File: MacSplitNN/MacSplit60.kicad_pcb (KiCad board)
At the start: 2 copper layers, 166.1 x 112 mm, 73 parts, among them J1 USB_C_Receptacle_USB2.0, SW1 SW_Push, SW10 SW_Push, SW100 SW_SPST, SW11 SW_Push, SW12 SW_Push, SW13 SW_Push, SW14 SW_Push, SW15 SW_Push, SW16 SW_Push, SW17 SW_Push, SW18 SW_Push, SW19 SW_Push, SW2 SW_Push, SW20 SW_Push, SW21 SW_Push, SW22 SW_Push, SW23 SW_Push, SW24 SW_Push, SW25 SW_Push, SW26 SW_Push, SW27 SW_Push, SW28 SW_Push, SW29 SW_Push, SW3 SW_Push, SW30 SW_Push, SW4 SW_Push, SW5 SW_Push, SW6 SW_Push, SW7 SW_Push, SW8 SW_Push, SW9 SW_Push, U1 Pico, U2 MCP23S17_ML

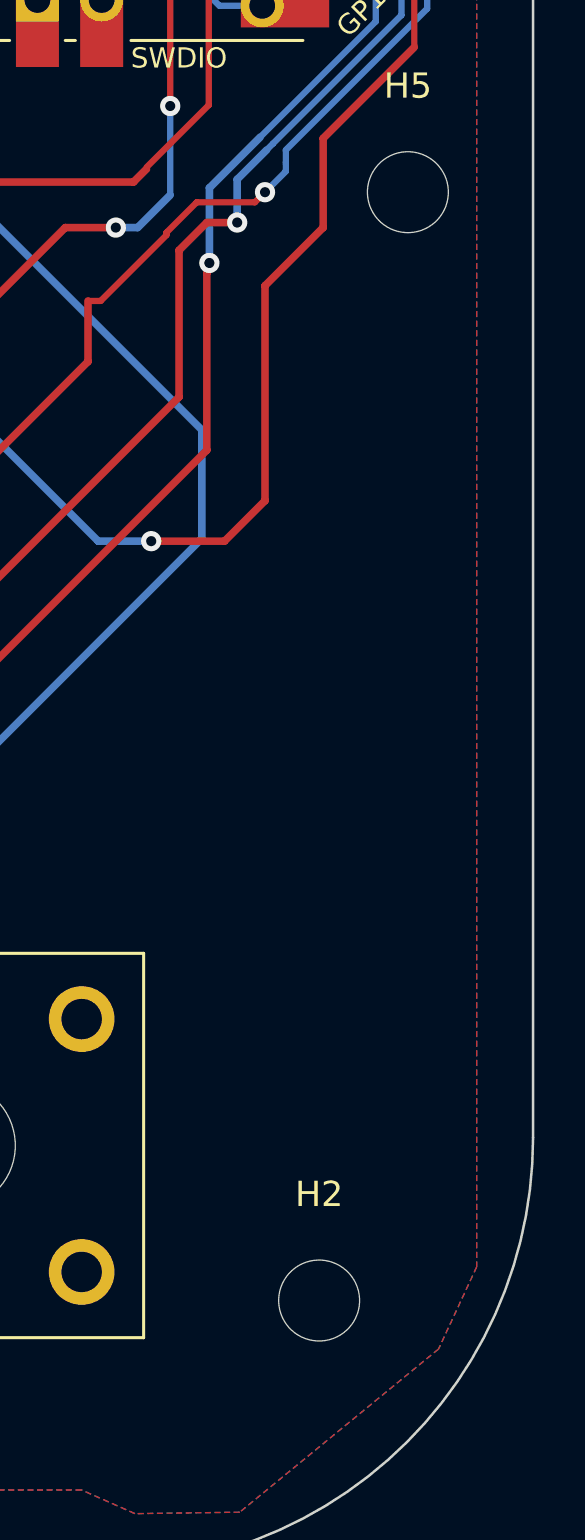
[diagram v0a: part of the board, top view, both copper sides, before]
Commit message: Adds PCB design info to silkscreen, gerbers for production
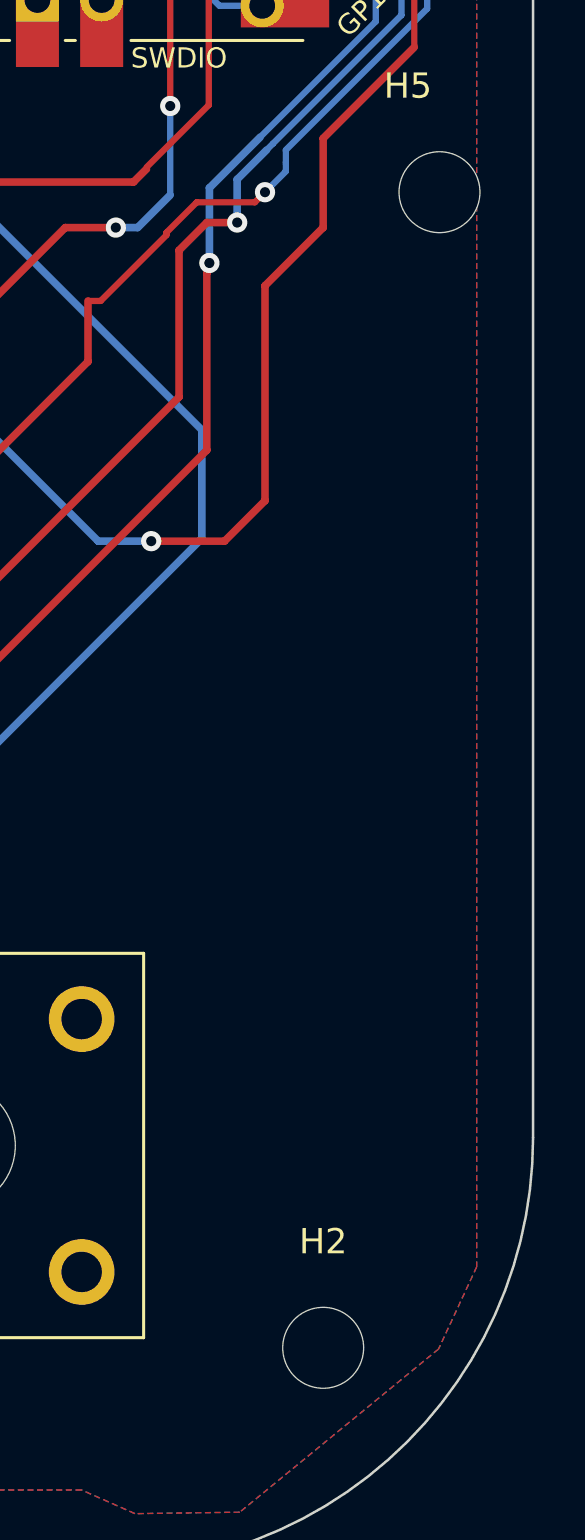
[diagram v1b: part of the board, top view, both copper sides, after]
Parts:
- moved H2 1.88 mm to (244.3, 138.3)
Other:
- board text added: "MacSplit60 Keyboard by Neeraj Adsul Copyright 2022, 125 Systems. Revision 1"
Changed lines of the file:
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@@
       (outputformat 1)
       (mirror false)
-      (drillshape 1)
+      (drillshape 0)
       (scaleselection 1)
       (outputdirectory "")
@@
   )
   (footprint "MountingHole:MountingHole_3.2mm_M3" (layer "F.Cu")
-    (at 244.14 136.43)
+    (at 244.3 138.3)
     (descr "Mounting Hole 3.2mm, no annular, M3")
     (tags "mounting hole 3.2mm no annular m3")
@@
     (fp_circle (center 0 0) (end 3.2 0) (layer "Cmts.User") (width 0.15) (fill none))
     (fp_circle (center 0 0) (end 3.45 0) (layer "F.CrtYd") (width 0.05) (fill none))
-    (pad "" np_thru_hole circle (at 0 0) (size 3.2 3.2) (drill 3.2) (layers *.Cu *.Mask))
+    (pad "" np_thru_hole circle (at 1.25 0) (size 3.2 3.2) (drill 3.2) (layers F&B.Cu *.Mask))
   )
   (footprint "Switch_Keyboard_Kailh:SW_Kailh_Choc_V1V2_1.00u" (layer "F.Cu")
@@
       (effects (font (size 1 1) (thickness 0.15)))
     )
-    (fp_text user "${REFERENCE}" (at 0 0) (layer "F.Fab")
+    (fp_text user "${REFERENCE}" (at 0 -1.2825) (layer "F.Fab")
       (effects (font (size 1 1) (thickness 0.15)))
     )
@@
     (fp_line (start -3 2) (end -2 3) (layer "B.Fab") (width 0.1))
     (fp_line (start 3 3) (end 3 -3) (layer "B.Fab") (width 0.1))
-    (pad "" smd roundrect (at 1.42 1.42) (size 1.14 1.14) (layers "B.Paste") (roundrect_rratio 0.219298))
-    (pad "" smd roundrect (at 1.42 0) (size 1.14 1.14) (layers "B.Paste") (roundrect_rratio 0.219298))
-    (pad "" smd roundrect (at 1.42 -1.42) (size 1.14 1.14) (layers "B.Paste") (roundrect_rratio 0.219298))
-    (pad "" smd roundrect (at 0 0) (size 1.14 1.14) (layers "B.Paste") (roundrect_rratio 0.219298))
-    (pad "" smd roundrect (at -1.42 1.42) (size 1.14 1.14) (layers "B.Paste") (roundrect_rratio 0.219298))
-    (pad "" smd roundrect (at 0 1.42) (size 1.14 1.14) (layers "B.Paste") (roundrect_rratio 0.219298))
-    (pad "" smd roundrect (at -1.42 -1.42) (size 1.14 1.14) (layers "B.Paste") (roundrect_rratio 0.219298))
-    (pad "" smd roundrect (at -1.42 0) (size 1.14 1.14) (layers "B.Paste") (roundrect_rratio 0.219298))
-    (pad "" smd roundrect (at 0 -1.42) (size 1.14 1.14) (layers "B.Paste") (roundrect_rratio 0.219298))
+    (pad "" smd roundrect (at 1.42 1.42) (size 1.14 1.14) (layers "B.Paste") (roundrect_rratio 0.2192982456))
+    (pad "" smd roundrect (at 1.42 0) (size 1.14 1.14) (layers "B.Paste") (roundrect_rratio 0.2192982456))
+    (pad "" smd roundrect (at 1.42 -1.42) (size 1.14 1.14) (layers "B.Paste") (roundrect_rratio 0.2192982456))
+    (pad "" smd roundrect (at 0 0) (size 1.14 1.14) (layers "B.Paste") (roundrect_rratio 0.2192982456))
+    (pad "" smd roundrect (at -1.42 1.42) (size 1.14 1.14) (layers "B.Paste") (roundrect_rratio 0.2192982456))
+    (pad "" smd roundrect (at 0 1.42) (size 1.14 1.14) (layers "B.Paste") (roundrect_rratio 0.2192982456))
+    (pad "" smd roundrect (at -1.42 -1.42) (size 1.14 1.14) (layers "B.Paste") (roundrect_rratio 0.2192982456))
+    (pad "" smd roundrect (at -1.42 0) (size 1.14 1.14) (layers "B.Paste") (roundrect_rratio 0.2192982456))
+    (pad "" smd roundrect (at 0 -1.42) (size 1.14 1.14) (layers "B.Paste") (roundrect_rratio 0.2192982456))
     (pad "1" smd roundrect (at -2.8375 1.95) (size 1.025 0.3) (layers "B.Cu" "B.Paste" "B.Mask") (roundrect_rratio 0.25)
       (net 28 "/ROW_4") (pinfunction "GPB4") (pintype "bidirectional"))
@@
     (effects (font (size 2 2) (thickness 0.15)))
   )
-  (target plus (at 172.3 39.3) (size 5) (width 0.1) (layer "Edge.Cuts"))
+  (gr_text "MacSplit60 Keyboard by Neeraj Adsul\nCopyright 2022, 125 Systems.\nRevision 1" (at 133.3 44.6) (layer "F.Fab")
+    (effects (font (size 2 2) (thickness 0.25)))
+  )
+  (target plus (at 172.3 39.6) (size 5) (width 0.1) (layer "Edge.Cuts"))
   (segment (start 190.725 42.775) (end 190.725 44.125) (width 0.3) (layer "F.Cu") (net 1))
   (segment (start 196.675 42.775) (end 196.675 44.125) (width 0.3) (layer "F.Cu") (net 1))

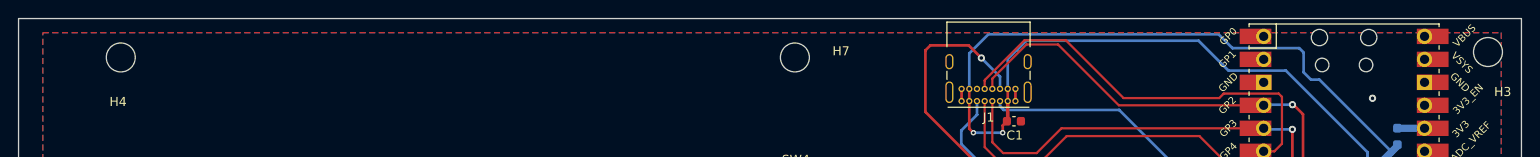
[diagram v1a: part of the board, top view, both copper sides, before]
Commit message: Changes USB-C footprint to circular hole and pad
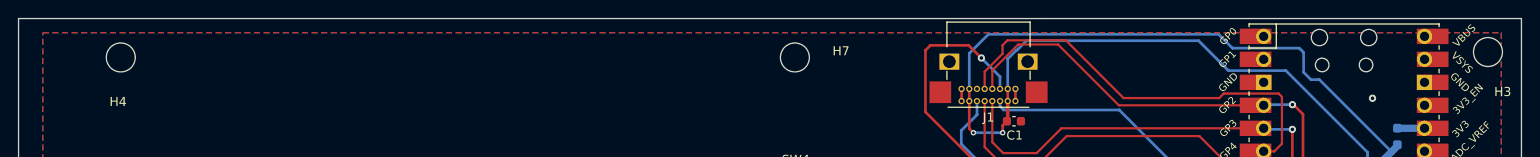
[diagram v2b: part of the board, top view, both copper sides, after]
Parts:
- J1: footprint Connector_USB:USB_C_Receptacle_GCT_USB4085 -> Connector_USB:USB_C_Receptacle_GCT_USB4085_Circular
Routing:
- net /SPI0_RX: track 74.6 -> 75.7 mm
- net /SPI0_SCK: track 71.0 -> 71.5 mm
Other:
- outline, holes or cut-outs redrawn
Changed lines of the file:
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@@
     )
   )
-  (footprint "Connector_USB:USB_C_Receptacle_GCT_USB4085" (layer "F.Cu")
+  (footprint "Connector_USB:USB_C_Receptacle_GCT_USB4085_Circular" (layer "F.Cu")
     (at 196.675 44.125 180)
     (descr "USB 2.0 Type C Receptacle, https://gct.co/Files/Drawings/USB4085.pdf")
@@
     (property "Sheetname" "")
     (attr through_hole)
-    (fp_text reference "J1" (at 2.975 -1.8) (layer "F.SilkS")
+    (fp_text reference "J1" (at 2.975 -1.8 180) (layer "F.SilkS")
       (effects (font (size 1 1) (thickness 0.15)))
     )
-    (fp_text value "USB_C_Receptacle_USB2.0" (at 2.975 9.925) (layer "F.Fab")
+    (fp_text value "USB_C_Receptacle_USB2.0" (at 2.975 9.925 180) (layer "F.Fab")
       (effects (font (size 1 1) (thickness 0.15)))
     )
-    (fp_text user "PCB Edge" (at 2.975 6.1) (layer "Dwgs.User")
+    (fp_text user "PCB Edge" (at 2.975 6.1 180) (layer "Dwgs.User")
       (effects (font (size 0.5 0.5) (thickness 0.1)))
     )
-    (fp_text user "${REFERENCE}" (at 2.975 4.025) (layer "F.Fab")
+    (fp_text user "${REFERENCE}" (at 2.975 4.025 180) (layer "F.Fab")
       (effects (font (size 1 1) (thickness 0.15)))
     )
-    (fp_line (start -1.62 8.73) (end 7.57 8.73) (layer "F.SilkS") (width 0.12))
     (fp_line (start 7.57 2.4) (end 7.57 3.3) (layer "F.SilkS") (width 0.12))
+    (fp_line (start -1.62 8.73) (end 7.57 8.73) (layer "F.SilkS") (width 0.12))
+    (fp_line (start -1.62 2.4) (end -1.62 3.3) (layer "F.SilkS") (width 0.12))
     (fp_line (start -1.62 6) (end -1.62 8.73) (layer "F.SilkS") (width 0.12))
     (fp_line (start -1.5 -0.68) (end 7.45 -0.68) (layer "F.SilkS") (width 0.12))
-    (fp_line (start -1.62 2.4) (end -1.62 3.3) (layer "F.SilkS") (width 0.12))
     (fp_line (start 7.57 6) (end 7.57 8.73) (layer "F.SilkS") (width 0.12))
+    (fp_line (start -2.3 9.11) (end 8.25 9.11) (layer "F.CrtYd") (width 0.05))
     (fp_line (start -2.3 -1.06) (end 8.25 -1.06) (layer "F.CrtYd") (width 0.05))
     (fp_line (start 8.25 -1.06) (end 8.25 9.11) (layer "F.CrtYd") (width 0.05))
     (fp_line (start -2.3 -1.06) (end -2.3 9.11) (layer "F.CrtYd") (width 0.05))
-    (fp_line (start -2.3 9.11) (end 8.25 9.11) (layer "F.CrtYd") (width 0.05))
     (fp_line (start -1.5 8.61) (end 7.45 8.61) (layer "F.Fab") (width 0.1))
-    (fp_line (start 7.45 -0.56) (end 7.45 8.61) (layer "F.Fab") (width 0.1))
-    (fp_line (start -0.025 6.1) (end 5.975 6.1) (layer "F.Fab") (width 0.1))
     (fp_line (start -1.5 -0.56) (end -1.5 8.61) (layer "F.Fab") (width 0.1))
     (fp_line (start -1.5 -0.56) (end 7.45 -0.56) (layer "F.Fab") (width 0.1))
+    (fp_line (start 7.45 -0.56) (end 7.45 8.61) (layer "F.Fab") (width 0.1))
+    (fp_line (start -0.025 6.1) (end 5.975 6.1) (layer "F.Fab") (width 0.1))
     (pad "A1" thru_hole circle (at 0 0 180) (size 0.7 0.7) (drill 0.4) (layers *.Cu *.Mask)
       (net 1 "GND") (pinfunction "GND") (pintype "passive"))
@@
     (pad "B12" thru_hole circle (at 0 1.35 180) (size 0.7 0.7) (drill 0.4) (layers *.Cu *.Mask)
       (net 1 "GND") (pinfunction "GND") (pintype "passive"))
-    (pad "S1" thru_hole oval (at -1.35 4.36 180) (size 0.9 1.7) (drill oval 0.6 1.4) (layers *.Cu *.Mask)
+    (pad "S1" thru_hole rect (at -1.35 4.36 180) (size 2.2 1.8) (drill 1.4) (layers *.Cu *.Mask)
       (net 1 "GND") (pinfunction "SHIELD") (pintype "passive"))
-    (pad "S1" thru_hole oval (at 7.3 4.36 180) (size 0.9 1.7) (drill oval 0.6 1.4) (layers *.Cu *.Mask)
+    (pad "S1" smd rect (at -1.35 0.98 180) (size 2.4 2.4) (drill oval (offset -1 0)) (layers "F.Cu" "F.Paste" "F.Mask")
       (net 1 "GND") (pinfunction "SHIELD") (pintype "passive"))
-    (pad "S1" thru_hole oval (at -1.35 0.98 180) (size 0.9 2.4) (drill oval 0.6 2.1) (layers *.Cu *.Mask)
+    (pad "S1" smd rect (at 7.3 0.98 180) (size 2.4 2.4) (drill oval (offset 1 0)) (layers "F.Cu" "F.Paste" "F.Mask")
       (net 1 "GND") (pinfunction "SHIELD") (pintype "passive"))
-    (pad "S1" thru_hole oval (at 7.3 0.98 180) (size 0.9 2.4) (drill oval 0.6 2.1) (layers *.Cu *.Mask)
+    (pad "S1" thru_hole rect (at 7.3 4.36 180) (size 2.2 1.8) (drill 1.4) (layers *.Cu *.Mask)
       (net 1 "GND") (pinfunction "SHIELD") (pintype "passive"))
     (model "${KICAD6_3DMODEL_DIR}/Connector_USB.3dshapes/USB_C_Receptacle_GCT_USB4085.wrl"
@@
   (gr_line (start 86.5 35) (end 86.5 109) (layer "Edge.Cuts") (width 0.1))
   (gr_line (start 252.6 130) (end 252.6 35) (layer "Edge.Cuts") (width 0.1))
+  (gr_line (start 200.05 35) (end 86.5 35) (layer "Edge.Cuts") (width 0.1))
   (gr_line (start 124.5 147) (end 235.6 147) (layer "Edge.Cuts") (width 0.1))
-  (gr_line (start 252.6 35) (end 86.5 35) (layer "Edge.Cuts") (width 0.1))
+  (gr_line (start 252.6 35) (end 200.05 35) (layer "Edge.Cuts") (width 0.1))
   (gr_arc (start 124.5 147) (mid 97.629942 135.870058) (end 86.5 109) (layer "Edge.Cuts") (width 0.1))
   (gr_text "RIGHT" (at 245.6 124.8) (layer "B.Mask")
@@
     (effects (font (size 2 2) (thickness 0.25)))
   )
-  (target plus (at 172.3 39.6) (size 5) (width 0.1) (layer "Edge.Cuts"))
+  (target plus (at 172.3 39.3) (size 5) (width 0.1) (layer "Edge.Cuts"))
   (segment (start 190.725 42.775) (end 190.725 44.125) (width 0.3) (layer "F.Cu") (net 1))
   (segment (start 196.675 42.775) (end 196.675 44.125) (width 0.3) (layer "F.Cu") (net 1))
@@
   (segment (start 230.2625 73.2275) (end 230.43 73.06) (width 0.3) (layer "B.Cu") (net 30))
   (segment (start 225.98 55.83) (end 225.98 53.12) (width 0.3) (layer "B.Cu") (net 30))
-  (segment (start 193.3 41.78) (end 197.67 37.41) (width 0.25) (layer "F.Cu") (net 31))
-  (segment (start 193.3 41.86) (end 193.3 41.78) (width 0.25) (layer "F.Cu") (net 31))
-  (segment (start 197.67 37.41) (end 202.25 37.41) (width 0.25) (layer "F.Cu") (net 31))
-  (segment (start 226.13 43.65) (end 226.13 48.83) (width 0.25) (layer "F.Cu") (net 31))
+  (segment (start 195.25 38.9) (end 195.25 37.95) (width 0.25) (layer "F.Cu") (net 31))
   (segment (start 225.77 43.29) (end 226.13 43.65) (width 0.25) (layer "F.Cu") (net 31))
-  (segment (start 202.25 37.41) (end 208.63 43.79) (width 0.25) (layer "F.Cu") (net 31))
-  (segment (start 193.275 42.775) (end 193.275 41.885) (width 0.25) (layer "F.Cu") (net 31))
-  (segment (start 219.2 43.79) (end 219.7 43.29) (width 0.25) (layer "F.Cu") (net 31))
-  (segment (start 193.275 41.885) (end 193.3 41.86) (width 0.25) (layer "F.Cu") (net 31))
-  (segment (start 224.12 49.68) (end 224.11 49.67) (width 0.25) (layer "F.Cu") (net 31))
-  (segment (start 225.28 49.68) (end 224.12 49.68) (width 0.25) (layer "F.Cu") (net 31))
   (segment (start 226.13 48.83) (end 225.28 49.68) (width 0.25) (layer "F.Cu") (net 31))
+  (segment (start 224.12 49.68) (end 224.11 49.67) (width 0.25) (layer "F.Cu") (net 31))
   (segment (start 219.7 43.29) (end 225.77 43.29) (width 0.25) (layer "F.Cu") (net 31))
+  (segment (start 219.2 43.79) (end 219.7 43.29) (width 0.25) (layer "F.Cu") (net 31))
+  (segment (start 193.275 40.875) (end 195.25 38.9) (width 0.25) (layer "F.Cu") (net 31))
+  (segment (start 226.13 43.65) (end 226.13 48.83) (width 0.25) (layer "F.Cu") (net 31))
+  (segment (start 225.28 49.68) (end 224.12 49.68) (width 0.25) (layer "F.Cu") (net 31))
+  (segment (start 202.25 37.41) (end 208.63 43.79) (width 0.25) (layer "F.Cu") (net 31))
+  (segment (start 193.275 42.775) (end 193.275 40.875) (width 0.25) (layer "F.Cu") (net 31))
+  (segment (start 195.79 37.41) (end 202.25 37.41) (width 0.25) (layer "F.Cu") (net 31))
+  (segment (start 195.25 37.95) (end 195.79 37.41) (width 0.25) (layer "F.Cu") (net 31))
   (segment (start 208.63 43.79) (end 219.2 43.79) (width 0.25) (layer "F.Cu") (net 31))
   (segment (start 232.45 58.01) (end 224.11 49.67) (width 0.3) (layer "B.Cu") (net 31))
   (segment (start 232.45 74.6225) (end 232.45 58.01) (width 0.3) (layer "B.Cu") (net 31))
-  (segment (start 201.39 37.87) (end 197.89 37.87) (width 0.25) (layer "F.Cu") (net 32))
   (segment (start 228.46 45.58) (end 227.37 44.49) (width 0.3) (layer "F.Cu") (net 32))
+  (segment (start 224.11 44.59) (end 208.11 44.59) (width 0.25) (layer "F.Cu") (net 32))
   (segment (start 227.34 44.52) (end 227.29 44.52) (width 0.3) (layer "F.Cu") (net 32))
+  (segment (start 201.39 37.87) (end 196.98 37.87) (width 0.25) (layer "F.Cu") (net 32))
   (segment (start 227.8 55.98) (end 228.46 55.32) (width 0.3) (layer "F.Cu") (net 32))
-  (segment (start 208.11 44.59) (end 201.39 37.87) (width 0.25) (layer "F.Cu") (net 32))
-  (segment (start 224.11 44.59) (end 208.11 44.59) (width 0.25) (layer "F.Cu") (net 32))
   (segment (start 228.46 55.32) (end 228.46 51.74) (width 0.3) (layer "F.Cu") (net 32))
-  (segment (start 194.125 41.635) (end 194.125 42.775) (width 0.25) (layer "F.Cu") (net 32))
-  (segment (start 197.89 37.87) (end 194.125 41.635) (width 0.25) (layer "F.Cu") (net 32))
   (segment (start 228.46 51.74) (end 228.46 45.58) (width 0.3) (layer "F.Cu") (net 32))
   (segment (start 227.37 44.49) (end 227.34 44.52) (width 0.3) (layer "F.Cu") (net 32))
+  (segment (start 208.11 44.59) (end 201.39 37.87) (width 0.25) (layer "F.Cu") (net 32))
+  (segment (start 194.125 40.725) (end 194.125 42.775) (width 0.25) (layer "F.Cu") (net 32))
+  (segment (start 196.98 37.87) (end 194.125 40.725) (width 0.25) (layer "F.Cu") (net 32))
   (via (at 227.8 55.98) (size 0.8) (drill 0.4) (layers "F.Cu" "B.Cu") (net 32))
   (via (at 227.29 44.52) (size 0.8) (drill 0.4) (layers "F.Cu" "B.Cu") (net 32))
